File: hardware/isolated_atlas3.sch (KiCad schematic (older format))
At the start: 17 parts, among them J501 CONN_01X02, P5 ATLAS_DO_PROBE, U501 ADM3260, U502 ATLAS_DO

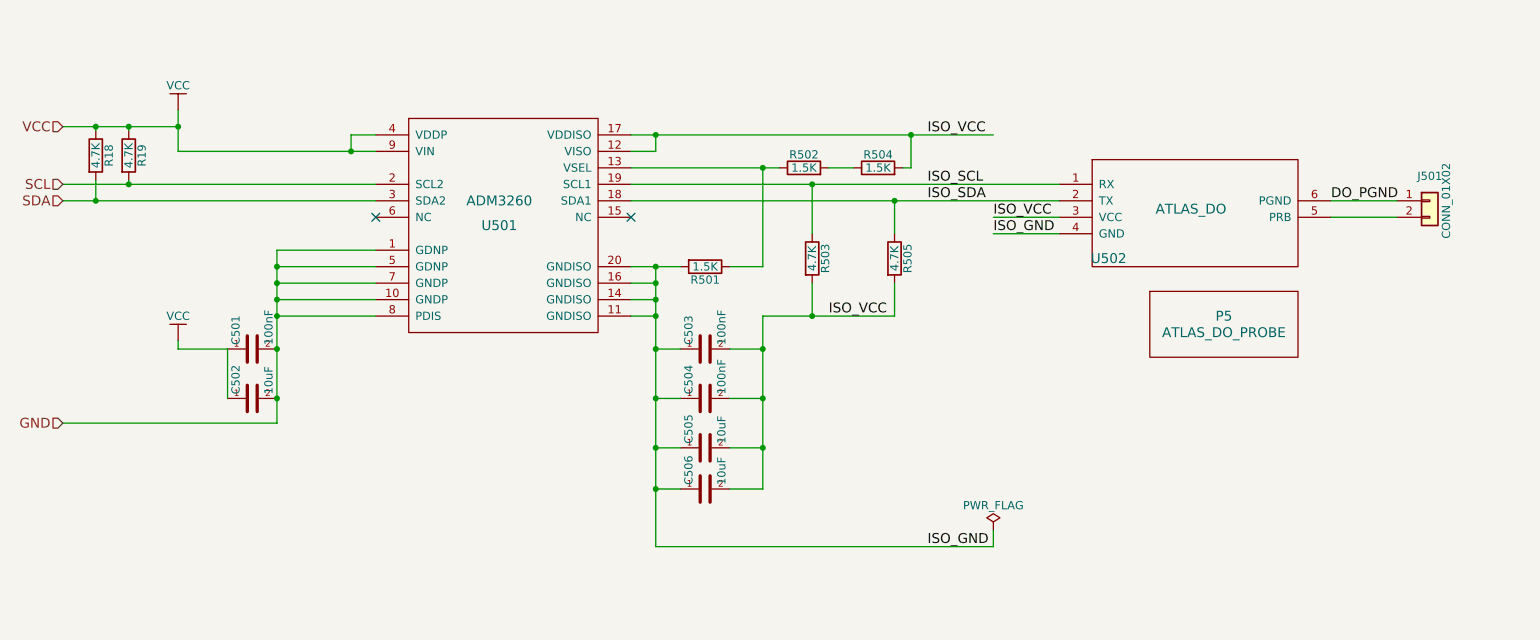
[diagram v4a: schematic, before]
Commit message: Generated panelized version of v0.11, including gerbers
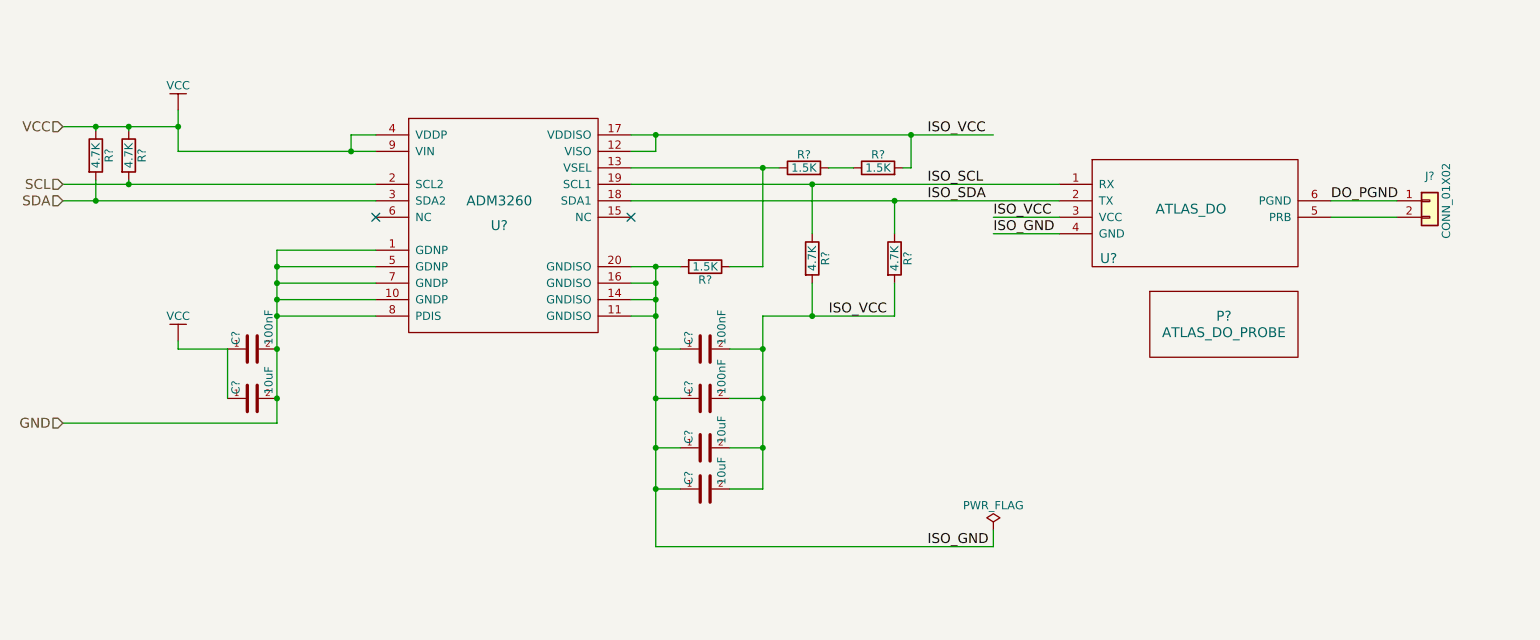
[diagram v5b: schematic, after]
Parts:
- renumbered C501 to C?, C502 to C?, C503 to C?, C504 to C?, C505 to C?, C506 to C?, J501 to J?, P5 to P?, R501 to R?, R502 to R?, R504 to R?, R503 to R?, R505 to R?, R18 to R?, R19 to R?, U501 to U?, U502 to U?
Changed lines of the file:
@@
 $EndDescr
 $Comp
-L fk-atlas-rescue:ADM3260-conservify U501
+L fk-atlas-rescue:ADM3260-conservify U?
 U 1 1 594C2CF0
 P 4400 2900
-F 0 "U501" H 4400 2750 60  0000 C CNN
+F 0 "U?" H 4400 2750 60  0000 C CNN
 F 1 "ADM3260" H 4400 2900 60  0000 C CNN
 F 2 "conservify:SSOP20-53" H 4400 2900 60  0001 C CNN
@@
 $EndComp
 $Comp
-L fk-atlas-rescue:CAPACITOR_CERAMIC-conservify C503
+L fk-atlas-rescue:CAPACITOR_CERAMIC-conservify C?
 U 1 1 594C2CF5
 P 5650 3800
-F 0 "C503" H 5675 3900 50  0000 L CNN
+F 0 "C?" H 5675 3900 50  0000 L CNN
 F 1 "100nF" H 5675 3700 50  0000 L CNN
 F 2 "conservify:CAP-0603" H 5688 3650 50  0001 C CNN
@@
 $EndComp
 $Comp
-L fk-atlas-rescue:CAPACITOR_CERAMIC-conservify C504
+L fk-atlas-rescue:CAPACITOR_CERAMIC-conservify C?
 U 1 1 594C2CF9
 P 5650 4100
-F 0 "C504" H 5675 4200 50  0000 L CNN
+F 0 "C?" H 5675 4200 50  0000 L CNN
 F 1 "100nF" H 5675 4000 50  0000 L CNN
 F 2 "conservify:CAP-0603" H 5688 3950 50  0001 C CNN
@@
 $EndComp
 $Comp
-L fk-atlas-rescue:CAPACITOR_CERAMIC-conservify C505
+L fk-atlas-rescue:CAPACITOR_CERAMIC-conservify C?
 U 1 1 594C2CFC
 P 5650 4400
-F 0 "C505" H 5675 4500 50  0000 L CNN
+F 0 "C?" H 5675 4500 50  0000 L CNN
 F 1 "10uF" H 5675 4300 50  0000 L CNN
 F 2 "conservify:CAP-0603" H 5688 4250 50  0001 C CNN
@@
 $EndComp
 $Comp
-L fk-atlas-rescue:CAPACITOR_CERAMIC-conservify C506
+L fk-atlas-rescue:CAPACITOR_CERAMIC-conservify C?
 U 1 1 594C2D00
 P 5650 4650
-F 0 "C506" H 5675 4750 50  0000 L CNN
+F 0 "C?" H 5675 4750 50  0000 L CNN
 F 1 "10uF" H 5675 4550 50  0000 L CNN
 F 2 "conservify:CAP-0603" H 5688 4500 50  0001 C CNN
@@
 $EndComp
 $Comp
-L fk-atlas-rescue:CAPACITOR_CERAMIC-conservify C501
+L fk-atlas-rescue:CAPACITOR_CERAMIC-conservify C?
 U 1 1 5948D5F5
 P 2900 3800
-F 0 "C501" H 2925 3900 50  0000 L CNN
+F 0 "C?" H 2925 3900 50  0000 L CNN
 F 1 "100nF" H 2925 3700 50  0000 L CNN
 F 2 "conservify:CAP-0603" H 2938 3650 50  0001 C CNN
@@
 $EndComp
 $Comp
-L fk-atlas-rescue:CAPACITOR_CERAMIC-conservify C502
+L fk-atlas-rescue:CAPACITOR_CERAMIC-conservify C?
 U 1 1 5948D68D
 P 2900 4100
-F 0 "C502" H 2925 4200 50  0000 L CNN
+F 0 "C?" H 2925 4200 50  0000 L CNN
 F 1 "10uF" H 2925 4000 50  0000 L CNN
 F 2 "conservify:CAP-0603" H 2938 3950 50  0001 C CNN
@@
 $EndComp
 $Comp
-L fk-atlas-rescue:R-conservify R501
+L fk-atlas-rescue:R-conservify R?
 U 1 1 594C2D0D
 P 5650 3300
-F 0 "R501" V 5730 3300 50  0000 C CNN
+F 0 "R?" V 5730 3300 50  0000 C CNN
 F 1 "1.5K" V 5650 3300 50  0000 C CNN
 F 2 "conservify:RES-0603" V 5580 3300 50  0001 C CNN
@@
 $EndComp
 $Comp
-L fk-atlas-rescue:R-conservify R502
+L fk-atlas-rescue:R-conservify R?
 U 1 1 594C2D11
 P 6250 2700
-F 0 "R502" V 6330 2700 50  0000 C CNN
+F 0 "R?" V 6330 2700 50  0000 C CNN
 F 1 "1.5K" V 6250 2700 50  0000 C CNN
 F 2 "conservify:RES-0603" V 6180 2700 50  0001 C CNN
@@
 $EndComp
 $Comp
-L fk-atlas-rescue:R-conservify R504
+L fk-atlas-rescue:R-conservify R?
 U 1 1 594C2D15
 P 6700 2700
-F 0 "R504" V 6780 2700 50  0000 C CNN
+F 0 "R?" V 6780 2700 50  0000 C CNN
 F 1 "1.5K" V 6700 2700 50  0000 C CNN
 F 2 "conservify:RES-0603" V 6630 2700 50  0001 C CNN
@@
 $EndComp
 $Comp
-L fk-atlas-rescue:R-conservify R503
+L fk-atlas-rescue:R-conservify R?
 U 1 1 594C2D19
 P 6300 3250
-F 0 "R503" V 6380 3250 50  0000 C CNN
+F 0 "R?" V 6380 3250 50  0000 C CNN
 F 1 "4.7K" V 6300 3250 50  0000 C CNN
 F 2 "conservify:RES-0603" V 6230 3250 50  0001 C CNN
@@
 $EndComp
 $Comp
-L fk-atlas-rescue:R-conservify R505
+L fk-atlas-rescue:R-conservify R?
 U 1 1 594C2D1D
 P 6800 3250
-F 0 "R505" V 6880 3250 50  0000 C CNN
+F 0 "R?" V 6880 3250 50  0000 C CNN
 F 1 "4.7K" V 6800 3250 50  0000 C CNN
 F 2 "conservify:RES-0603" V 6730 3250 50  0001 C CNN
@@
 $EndComp
 $Comp
-L fk-atlas-rescue:VCC-conservify #PWR063
+L fk-atlas-rescue:VCC-conservify #PWR?
 U 1 1 5948EDC0
 P 2450 3750
-F 0 "#PWR063" H 2450 3600 50  0001 C CNN
+F 0 "#PWR?" H 2450 3600 50  0001 C CNN
 F 1 "VCC" H 2450 3900 50  0000 C CNN
 F 2 "" H 2450 3750 50  0001 C CNN
@@
 $EndComp
 $Comp
-L fk-atlas-rescue:VCC-conservify #PWR064
+L fk-atlas-rescue:VCC-conservify #PWR?
 U 1 1 5948EDF6
 P 2450 2350
-F 0 "#PWR064" H 2450 2200 50  0001 C CNN
+F 0 "#PWR?" H 2450 2200 50  0001 C CNN
 F 1 "VCC" H 2450 2500 50  0000 C CNN
 F 2 "" H 2450 2350 50  0001 C CNN
@@
 $EndComp
 $Comp
-L fk-atlas-rescue:ATLAS_SENSOR-conservify U502
+L fk-atlas-rescue:ATLAS_SENSOR-conservify U?
 U 1 1 594C2D34
 P 8550 2900
-F 0 "U502" H 8100 2550 60  0000 C CNN
+F 0 "U?" H 8100 2550 60  0000 C CNN
 F 1 "ATLAS_DO" H 8600 2850 60  0000 C CNN
 F 2 "conservify:ATLAS_SENSOR_BOARD_COMBO" H 8550 2900 60  0001 C CNN
@@
 $EndComp
 $Comp
-L fk-atlas-rescue:CONN_01x02-conservify J501
+L fk-atlas-rescue:CONN_01x02-conservify J?
 U 1 1 594D403D
 P 10050 2900
-F 0 "J501" H 10050 3050 50  0000 C CNN
+F 0 "J?" H 10050 3050 50  0000 C CNN
 F 1 "CONN_01X02" V 10150 2900 50  0000 C CNN
 F 2 "conservify:BNC" H 10050 2900 50  0001 C CNN
@@
 $EndComp
 $Comp
-L fk-atlas-rescue:ATLAS_WATER_PROBE-conservify P5
+L fk-atlas-rescue:ATLAS_WATER_PROBE-conservify P?
 U 1 1 59D2A6F4
 P 8800 3600
-F 0 "P5" H 8800 3600 60  0000 C CNN
+F 0 "P?" H 8800 3600 60  0000 C CNN
 F 1 "ATLAS_DO_PROBE" H 8800 3500 60  0000 C CNN
 F 2 "conservify:Dummy_Empty" H 8800 3600 60  0001 C CNN
@@
 $EndComp
 $Comp
-L fk-atlas-rescue:PWR_FLAG-conservify #FLG0108
+L fk-atlas-rescue:PWR_FLAG-conservify #FLG?
 U 1 1 5BCDA7BC
 P 7400 4900
-F 0 "#FLG0108" H 7400 4975 50  0001 C CNN
+F 0 "#FLG?" H 7400 4975 50  0001 C CNN
 F 1 "PWR_FLAG" H 7400 5050 50  0000 C CNN
 F 2 "" H 7400 4900 50  0001 C CNN
@@
 NoConn ~ 5200 3000
 $Comp
-L fk-atlas-rescue:R-conservify R18
+L fk-atlas-rescue:R-conservify R?
 U 1 1 5C7DFDFD
 P 1950 2625
-F 0 "R18" V 2030 2625 50  0000 C CNN
+F 0 "R?" V 2030 2625 50  0000 C CNN
 F 1 "4.7K" V 1950 2625 50  0000 C CNN
 F 2 "conservify:RES-0603" V 1880 2625 50  0001 C CNN
@@
 $EndComp
 $Comp
-L fk-atlas-rescue:R-conservify R19
+L fk-atlas-rescue:R-conservify R?
 U 1 1 5C7DFF29
 P 2150 2625
-F 0 "R19" V 2230 2625 50  0000 C CNN
+F 0 "R?" V 2230 2625 50  0000 C CNN
 F 1 "4.7K" V 2150 2625 50  0000 C CNN
 F 2 "conservify:RES-0603" V 2080 2625 50  0001 C CNN
